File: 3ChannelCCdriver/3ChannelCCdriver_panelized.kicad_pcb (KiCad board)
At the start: 2 copper layers, 100.5 x 100.5 mm, 412 parts, among them J1 BB10-10S-02, J2 Screw_Terminal_01x02, J3 Screw_Terminal_01x02, J4 Screw_Terminal_01x02, J5 Screw_Terminal_01x02, U1 AL8860WT-7, U2 AL8860WT-7, U3 AL8860WT-7, U4 TPS54202DDC, U5 XL6019, U6 ESP-12F, U7 XC6210B332MR

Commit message: Added documentation
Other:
- board text added: "JLCJLCJLCJLC"

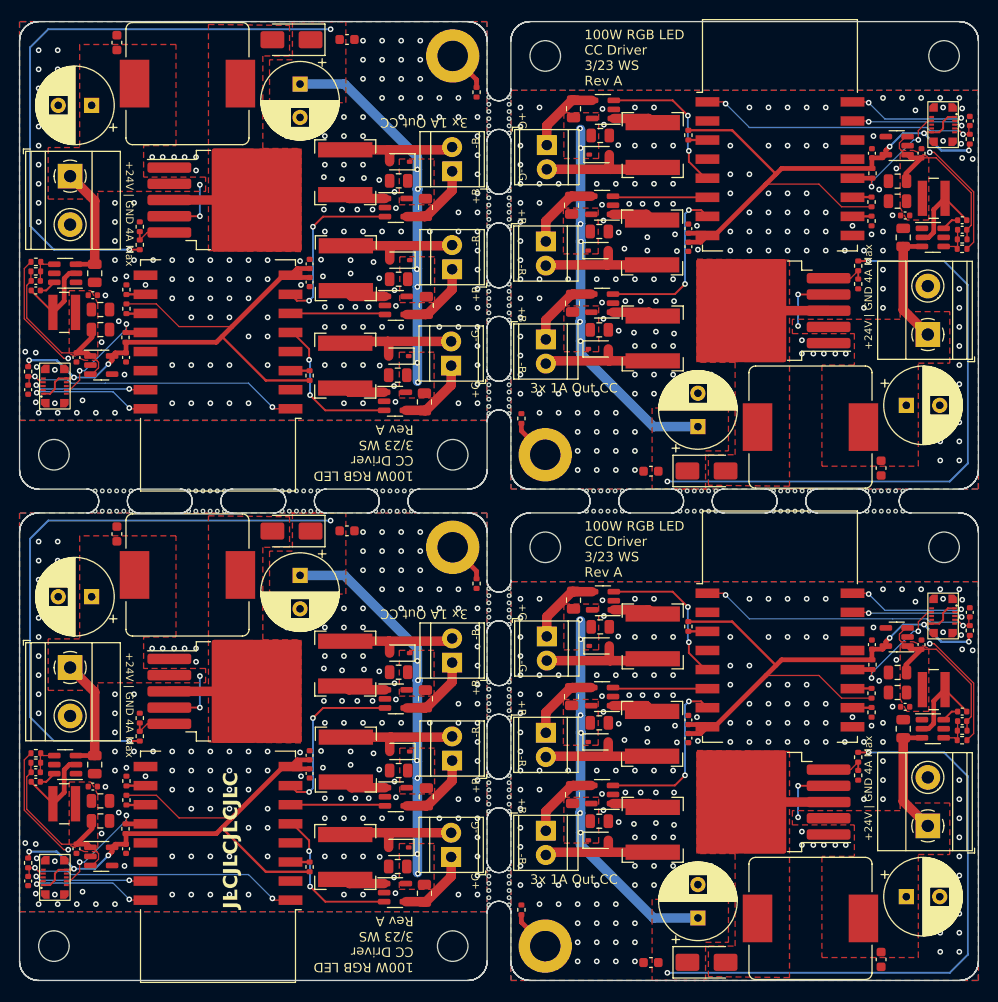
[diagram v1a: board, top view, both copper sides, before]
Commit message: changed panelization
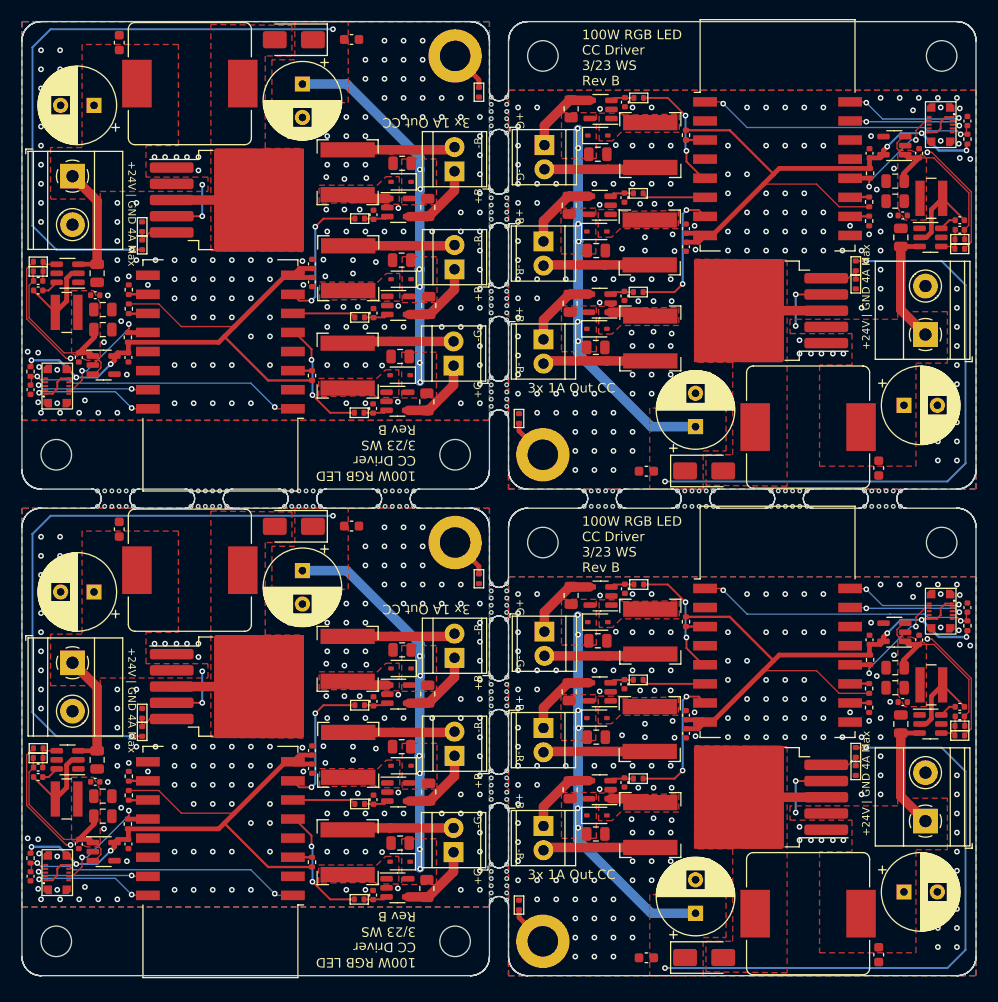
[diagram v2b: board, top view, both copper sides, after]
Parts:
- removed the C1 at (137.9, 57.1)
- removed the C1 at (159.1, 83.4)
- removed the C1 at (137.9, 108.6)
- removed the C1 at (159.1, 31.9)
- removed the C10 at (191.2, 60.2)
- removed the C10 at (105.8, 28.8)
- removed the C10 at (105.8, 80.3)
- removed the C10 at (191.2, 111.7)
- removed the C11 at (108.5, 73.7)
- removed the C11 at (108.5, 22.2)
- removed the C11 at (188.6, 118.3)
- removed the C11 at (188.6, 66.8)
- removed the C12 at (164.4, 118.6)
- removed the C12 at (132.6, 73.4)
- removed the C12 at (164.4, 67.1)
- removed the C12 at (132.6, 21.9)
- removed the C13 at (127.7, 26.5)
- removed the C13 at (127.7, 78.0)
- removed the C13 at (169.3, 114.0)
- removed the C13 at (169.3, 62.5)
- removed the C14 at (197.8, 30.4)
- removed the C14 at (197.8, 81.9)
- removed the C14 at (99.2, 58.6)
- removed the C14 at (99.2, 110.1)
- removed the C15 at (192.8, 85.3)
- removed the C15 at (104.2, 106.7)
- removed the C15 at (192.8, 33.8)
- removed the C15 at (104.2, 55.2)
- removed the C16 at (109.4, 55.2)
- removed the C16 at (187.6, 33.8)
- removed the C16 at (109.4, 106.7)
- removed the C16 at (187.6, 85.3)
- removed the C17 at (128.7, 45.4)
- removed the C17 at (128.7, 96.9)
- removed the C17 at (168.3, 43.6)
- removed the C17 at (168.3, 95.1)
- removed the C18 at (168.3, 93.2)
- removed the C18 at (168.3, 41.7)
- removed the C18 at (128.7, 98.8)
- removed the C18 at (128.7, 47.3)
- removed the C2 at (159.0, 93.5)
- removed the C2 at (138.0, 47.0)
- removed the C2 at (159.0, 42.0)
- removed the C2 at (138.0, 98.5)
- removed the C3 at (159.0, 52.3)
- removed the C3 at (159.0, 103.8)
- removed the C3 at (138.0, 88.2)
- removed the C3 at (138.0, 36.7)
- removed the C4 at (190.9, 94.1)
- removed the C4 at (190.9, 42.6)
- removed the C4 at (106.1, 46.4)
- removed the C4 at (106.1, 97.9)
- removed the C5 at (197.1, 92.3)
- removed the C5 at (100.0, 48.2)
- removed the C5 at (100.0, 99.7)
- removed the C5 at (197.1, 40.8)
- removed the C6 at (100.0, 98.7)
- removed the C6 at (197.1, 41.8)
- removed the C6 at (100.0, 47.2)
- removed the C6 at (197.1, 93.3)
- removed the C7 at (190.3, 88.2)
- removed the C7 at (106.7, 52.3)
- removed the C7 at (106.7, 103.8)
- removed the C7 at (190.3, 36.7)
- removed the C8 at (190.3, 90.3)
- removed the C8 at (106.7, 101.7)
- removed the C8 at (190.3, 38.8)
- removed the C8 at (106.7, 50.2)
- removed the C9 at (105.9, 100.2)
- removed the C9 at (191.1, 91.8)
- removed the C9 at (191.1, 40.3)
- removed the C9 at (105.9, 48.7)
- removed the D1 at (138.0, 106.6)
- removed the D1 at (159.0, 85.4)
- removed the D1 at (159.0, 33.9)
- removed the D1 at (138.0, 55.1)
- removed the D2 at (138.1, 96.5)
- removed the D2 at (138.1, 45.0)
- removed the D2 at (158.9, 44.0)
- removed the D2 at (158.9, 95.5)
- removed the D3 at (138.1, 34.7)
- removed the D3 at (158.9, 105.8)
- removed the D3 at (158.9, 54.3)
- removed the D3 at (138.1, 86.2)
- removed the D4 at (126.8, 73.4)
- removed the D4 at (170.2, 67.1)
- removed the D4 at (170.2, 118.6)
- removed the D4 at (126.8, 21.9)
- removed the H1 at (153.3, 116.9)
- removed the H1 at (153.3, 65.4)
- removed the H1 at (143.7, 23.6)
- removed the H1 at (143.7, 75.1)
- removed the H2 at (143.7, 116.9)
- removed the H2 at (153.3, 75.1)
- removed the H2 at (143.7, 65.4)
- removed the H2 at (153.3, 23.6)
- removed the H3 at (195.2, 75.1)
- removed the H3 at (195.2, 23.6)
- removed the H3 at (101.8, 116.9)
- removed the H3 at (101.8, 65.4)
- removed the J1 at (195.1, 30.8)
- removed the J1 at (195.1, 82.3)
- removed the J1 at (102.0, 58.2)
- removed the J1 at (102.0, 109.7)
- removed the J2 at (193.4, 52.8)
- removed the J2 at (103.5, 36.2)
- removed the J2 at (103.5, 87.7)
- removed the J2 at (193.4, 104.3)
- removed the J3 at (153.4, 94.5)
- removed the J3 at (153.4, 43.0)
- removed the J3 at (143.6, 97.5)
- removed the J3 at (143.6, 46.0)
- removed the J4 at (153.4, 104.8)
- removed the J4 at (143.6, 35.7)
- removed the J4 at (153.4, 53.3)
- removed the J4 at (143.6, 87.2)
- removed the J5 at (153.5, 32.9)
- removed the J5 at (143.5, 56.1)
- removed the J5 at (143.5, 107.6)
- removed the J5 at (153.5, 84.4)
- removed the L1 at (132.4, 56.1)
- removed the L1 at (164.6, 84.4)
- removed the L1 at (132.4, 107.6)
- removed the L1 at (164.6, 32.9)
- removed the L2 at (132.4, 45.9)
- removed the L2 at (132.4, 97.4)
- removed the L2 at (164.6, 43.1)
- removed the L2 at (164.6, 94.7)
- removed the L3 at (164.6, 53.2)
- removed the L3 at (164.6, 104.7)
- removed the L3 at (132.4, 87.3)
- removed the L3 at (132.4, 35.8)
- removed the L4 at (194.1, 38.5)
- removed the L4 at (102.9, 102.0)
- removed the L4 at (102.9, 50.5)
- removed the L4 at (194.1, 90.0)
- removed the L5 at (181.2, 114.0)
- removed the L5 at (115.8, 26.5)
- removed the L5 at (115.8, 78.0)
- removed the L5 at (181.2, 62.5)
- removed the R1 at (140.7, 111.4)
- removed the R1 at (156.3, 80.6)
- removed the R1 at (140.7, 59.9)
- removed the R1 at (156.3, 29.1)
- removed the R12 at (99.2, 56.7)
- removed the R12 at (197.8, 32.3)
- removed the R12 at (99.2, 108.2)
- removed the R12 at (197.8, 83.8)
- removed the R13 at (168.3, 83.4)
- removed the R13 at (168.3, 31.9)
- removed the R13 at (128.7, 108.6)
- removed the R13 at (128.7, 57.1)
- removed the R14 at (109.3, 53.1)
- removed the R14 at (187.7, 87.4)
- removed the R14 at (109.3, 104.6)
- removed the R14 at (187.7, 35.9)
- removed the R15 at (187.6, 38.9)
- removed the R15 at (187.6, 90.4)
- removed the R15 at (109.5, 50.1)
- removed the R15 at (109.5, 101.6)
- removed the R16 at (187.6, 40.9)
- removed the R16 at (187.6, 92.4)
- removed the R16 at (109.5, 99.6)
- removed the R16 at (109.5, 48.1)
- removed the R2 at (156.1, 39.2)
- removed the R2 at (140.9, 49.8)
- removed the R2 at (140.9, 101.3)
- removed the R2 at (156.1, 90.8)
- removed the R3 at (140.8, 91.0)
- removed the R3 at (156.2, 101.0)
- removed the R3 at (140.8, 39.5)
- removed the R3 at (156.2, 49.5)
- removed the R4 at (100.0, 97.7)
- removed the R4 at (100.0, 46.2)
- removed the R4 at (197.1, 42.8)
- removed the R4 at (197.1, 94.3)
- removed the R5 at (100.0, 96.7)
- removed the R5 at (100.0, 45.2)
- removed the R5 at (197.0, 95.3)
- removed the R5 at (197.0, 43.8)
- removed the R6 at (146.2, 78.9)
- removed the R6 at (146.2, 27.4)
- removed the R6 at (150.8, 61.6)
- removed the R6 at (150.8, 113.1)
- removed the R8 at (186.2, 45.6)
- removed the R8 at (110.8, 94.9)
- removed the R8 at (110.8, 43.4)
- removed the R8 at (186.2, 97.1)
- removed the R9 at (110.8, 93.0)
- removed the R9 at (186.2, 47.5)
- removed the R9 at (186.2, 99.0)
- removed the R9 at (110.8, 41.5)
- removed the REF** at (189.3, 69.2)
- removed the REF** at (167.5, 71.3)
- removed the REF** at (149.6, 111.1)
- removed the REF** at (149.6, 110.3)
- removed the REF** at (149.6, 100.5)
- removed the REF** at (147.4, 99.0)
- removed the REF** at (107.7, 69.2)
- removed the REF** at (179.5, 69.2)
- removed the REF** at (125.8, 71.3)
- removed the REF** at (178.0, 69.2)
- removed the REF** at (147.4, 29.4)
- removed the REF** at (157.7, 71.3)
- removed the REF** at (190.1, 71.3)
- removed the REF** at (149.6, 109.6)
- removed the REF** at (149.6, 80.9)
- removed the REF** at (160.7, 69.2)
- removed the REF** at (116.7, 71.3)
- removed the REF** at (147.4, 99.8)
- removed the REF** at (138.6, 69.2)
- removed the REF** at (147.4, 49.0)
- removed the REF** at (135.6, 69.2)
- removed the REF** at (161.4, 71.3)
- removed the REF** at (149.6, 108.8)
- removed the REF** at (149.6, 28.7)
- removed the REF** at (126.5, 71.3)
- removed the REF** at (147.4, 61.1)
- removed the REF** at (147.4, 82.4)
- removed the REF** at (147.4, 31.7)
- removed the REF** at (106.2, 69.2)
- removed the REF** at (147.4, 60.3)
- removed the REF** at (187.1, 69.2)
- removed the REF** at (147.4, 102.8)
- removed the REF** at (108.4, 71.3)
- removed the REF** at (116.0, 69.2)
- removed the REF** at (128.8, 71.3)
- removed the REF** at (147.4, 110.3)
- removed the REF** at (147.4, 40.7)
- removed the REF** at (187.1, 71.3)
- removed the REF** at (147.4, 89.2)
- removed the REF** at (137.1, 69.2)
- removed the REF** at (147.4, 59.6)
- removed the REF** at (147.4, 30.9)
- removed the REF** at (138.6, 71.3)
- removed the REF** at (119.7, 71.3)
- removed the REF** at (149.6, 47.5)
- removed the REF** at (128.0, 71.3)
- removed the REF** at (147.4, 37.7)
- removed the REF** at (109.2, 69.2)
- removed the REF** at (190.1, 69.2)
- removed the REF** at (106.2, 71.3)
- removed the REF** at (149.6, 39.2)
- removed the REF** at (128.0, 69.2)
- removed the REF** at (149.6, 30.2)
- removed the REF** at (147.4, 47.5)
- removed the REF** at (137.8, 71.3)
- removed the REF** at (149.6, 102.8)
- removed the REF** at (190.8, 69.2)
- removed the REF** at (167.5, 69.2)
- removed the REF** at (149.6, 102.0)
- removed the REF** at (168.2, 69.2)
- removed the REF** at (168.2, 71.3)
- removed the REF** at (171.2, 71.3)
- removed the REF** at (149.6, 80.2)
- removed the REF** at (149.6, 57.3)
- removed the REF** at (126.5, 69.2)
- removed the REF** at (147.4, 83.2)
- removed the REF** at (149.6, 81.7)
- removed the REF** at (147.4, 93.0)
- removed the REF** at (180.3, 69.2)
- removed the REF** at (149.6, 82.4)
- removed the REF** at (149.6, 31.7)
- removed the REF** at (147.4, 40.0)
- removed the REF** at (129.5, 69.2)
- removed the REF** at (147.4, 28.7)
- removed the REF** at (177.3, 71.3)
- removed the REF** at (149.6, 59.6)
- removed the REF** at (179.5, 71.3)
- removed the REF** at (149.6, 48.3)
- removed the REF** at (147.4, 79.4)
- removed the REF** at (147.4, 90.0)
- removed the REF** at (160.7, 71.3)
- removed the REF** at (169.7, 69.2)
- removed the REF** at (149.6, 61.1)
- removed the REF** at (149.6, 99.0)
- removed the REF** at (149.6, 93.0)
- removed the REF** at (159.9, 69.2)
- removed the REF** at (147.4, 102.0)
- removed the REF** at (181.0, 69.2)
- removed the REF** at (149.6, 49.8)
- removed the REF** at (149.6, 37.7)
- removed the REF** at (147.4, 50.5)
- removed the REF** at (117.5, 71.3)
- removed the REF** at (149.6, 51.3)
- removed the REF** at (188.6, 69.2)
- removed the REF** at (149.6, 99.8)
- removed the REF** at (136.3, 71.3)
- removed the REF** at (159.2, 71.3)
- removed the REF** at (147.4, 39.2)
- removed the REF** at (158.4, 69.2)
- removed the REF** at (181.0, 71.3)
- removed the REF** at (147.4, 100.5)
- removed the REF** at (149.6, 79.4)
- removed the REF** at (106.9, 69.2)
- removed the REF** at (137.1, 71.3)
- removed the REF** at (147.4, 109.6)
- removed the REF** at (147.4, 27.9)
- removed the REF** at (149.6, 27.9)
- removed the REF** at (147.4, 101.3)
- removed the REF** at (147.4, 58.8)
- removed the REF** at (119.0, 69.2)
- removed the REF** at (170.5, 69.2)
- removed the REF** at (149.6, 40.7)
- removed the REF** at (149.6, 91.5)
- removed the REF** at (169.0, 69.2)
- removed the REF** at (128.8, 69.2)
- removed the REF** at (116.7, 69.2)
- removed the REF** at (149.6, 38.5)
- removed the REF** at (147.4, 111.8)
- removed the REF** at (119.0, 71.3)
- removed the REF** at (149.6, 83.2)
- removed the REF** at (169.7, 71.3)
- removed the REF** at (147.4, 111.1)
- removed the REF** at (147.4, 49.8)
- removed the REF** at (107.7, 71.3)
- removed the REF** at (118.2, 69.2)
- removed the REF** at (147.4, 80.2)
- removed the REF** at (147.4, 38.5)
- removed the REF** at (149.6, 29.4)
- removed the REF** at (147.4, 92.2)
- removed the REF** at (147.4, 112.6)
- removed the REF** at (159.9, 71.3)
- removed the REF** at (178.8, 71.3)
- removed the REF** at (116.0, 71.3)
- removed the REF** at (147.4, 81.7)
- removed the REF** at (149.6, 58.8)
- removed the REF** at (177.3, 69.2)
- removed the REF** at (149.6, 41.5)
- removed the REF** at (137.8, 69.2)
- removed the REF** at (188.6, 71.3)
- removed the REF** at (169.0, 71.3)
- removed the REF** at (109.9, 69.2)
- removed the REF** at (149.6, 30.9)
- removed the REF** at (171.2, 69.2)
- removed the REF** at (178.8, 69.2)
- removed the REF** at (147.4, 57.3)
- removed the REF** at (106.9, 71.3)
- removed the REF** at (149.6, 89.2)
- removed the REF** at (149.6, 92.2)
- removed the REF** at (108.4, 69.2)
- removed the REF** at (136.3, 69.2)
- removed the REF** at (149.6, 90.7)
- removed the REF** at (117.5, 69.2)
- removed the REF** at (158.4, 71.3)
- removed the REF** at (127.3, 69.2)
- removed the REF** at (149.6, 58.1)
- removed the REF** at (127.3, 71.3)
- removed the REF** at (109.2, 71.3)
- removed the REF** at (170.5, 71.3)
- removed the REF** at (149.6, 112.6)
- removed the REF** at (147.4, 51.3)
- removed the REF** at (149.6, 101.3)
- removed the REF** at (149.6, 40.0)
- removed the REF** at (149.6, 90.0)
- removed the REF** at (147.4, 108.8)
- removed the REF** at (190.8, 71.3)
- removed the REF** at (187.8, 71.3)
- removed the REF** at (149.6, 60.3)
- removed the REF** at (139.3, 71.3)
- removed the REF** at (147.4, 41.5)
- removed the REF** at (118.2, 71.3)
- removed the REF** at (157.7, 69.2)
- removed the REF** at (149.6, 111.8)
- removed the REF** at (159.2, 69.2)
- removed the REF** at (147.4, 80.9)
- removed the REF** at (147.4, 58.1)
- removed the REF** at (149.6, 50.5)
- removed the REF** at (180.3, 71.3)
- removed the REF** at (147.4, 30.2)
- removed the REF** at (178.0, 71.3)
- removed the REF** at (161.4, 69.2)
- removed the REF** at (139.3, 69.2)
- removed the REF** at (149.6, 49.0)
- removed the REF** at (109.9, 71.3)
- removed the REF** at (147.4, 91.5)
- removed the REF** at (187.8, 69.2)
- removed the REF** at (189.3, 71.3)
- removed the REF** at (129.5, 71.3)
- removed the REF** at (147.4, 90.7)
- removed the REF** at (125.8, 69.2)
- removed the REF** at (147.4, 48.3)
- removed the REF** at (135.6, 71.3)
- removed the REF** at (119.7, 69.2)
- removed the U1 at (137.6, 111.3)
- removed the U1 at (137.6, 59.8)
- removed the U1 at (159.4, 29.2)
- removed the U1 at (159.4, 80.7)
- removed the U2 at (159.3, 90.8)
- removed the U2 at (159.3, 39.2)
- removed the U2 at (137.7, 49.8)
- removed the U2 at (137.7, 101.3)
- removed the U3 at (159.3, 101.0)
- removed the U3 at (137.7, 91.0)
- removed the U3 at (159.3, 49.5)
- removed the U3 at (137.7, 39.5)
- removed the U4 at (103.0, 46.4)
- removed the U4 at (194.0, 42.6)
- removed the U4 at (194.0, 94.1)
- removed the U4 at (103.0, 97.9)
- removed the U5 at (121.6, 38.7)
- removed the U5 at (121.6, 90.2)
- removed the U5 at (175.4, 50.3)
- removed the U5 at (175.4, 101.8)
- removed the U6 at (119.0, 57.1)
- removed the U6 at (177.9, 83.4)
- removed the U6 at (119.0, 108.6)
- removed the U6 at (177.9, 31.9)
- removed the U7 at (190.2, 33.0)
- removed the U7 at (106.8, 107.5)
- removed the U7 at (106.8, 56.0)
- removed the U7 at (190.2, 84.5)
- added C1: 0805,10uF,50V,X5R, Capacitor_SMD:C_0805_2012Metric, F.Cu at (158.9, 33.9)
- added C1: 0805,10uF,50V,X5R, Capacitor_SMD:C_0805_2012Metric, F.Cu at (138.1, 55.1)
- added C1: 0805,10uF,50V,X5R, Capacitor_SMD:C_0805_2012Metric, F.Cu at (158.9, 84.9)
- added C1: 0805,10uF,50V,X5R, Capacitor_SMD:C_0805_2012Metric, F.Cu at (138.1, 106.1)
- added C10: 220uF/50V, Capacitor_THT:CP_Radial_D8.0mm_P3.50mm, F.Cu at (106.1, 28.8)
- added C10: 220uF/50V, Capacitor_THT:CP_Radial_D8.0mm_P3.50mm, F.Cu at (190.9, 111.2)
- added C10: 220uF/50V, Capacitor_THT:CP_Radial_D8.0mm_P3.50mm, F.Cu at (190.9, 60.2)
- added C10: 220uF/50V, Capacitor_THT:CP_Radial_D8.0mm_P3.50mm, F.Cu at (106.1, 79.8)
- added C11: 0603,100nF,50V,X7R, Capacitor_SMD:C_0603_1608Metric, F.Cu at (188.3, 117.8)
- added C11: 0603,100nF,50V,X7R, Capacitor_SMD:C_0603_1608Metric, F.Cu at (108.7, 73.2)
- added C11: 0603,100nF,50V,X7R, Capacitor_SMD:C_0603_1608Metric, F.Cu at (108.7, 22.2)
- added C11: 0603,100nF,50V,X7R, Capacitor_SMD:C_0603_1608Metric, F.Cu at (188.3, 66.8)
- added C12: 0603,100nF,50V,X7R, Capacitor_SMD:C_0603_1608Metric, F.Cu at (133.1, 72.9)
- added C12: 0603,100nF,50V,X7R, Capacitor_SMD:C_0603_1608Metric, F.Cu at (133.1, 21.9)
- added C12: 0603,100nF,50V,X7R, Capacitor_SMD:C_0603_1608Metric, F.Cu at (163.9, 118.1)
- added C12: 0603,100nF,50V,X7R, Capacitor_SMD:C_0603_1608Metric, F.Cu at (163.9, 67.1)
- added C13: 220uF/50V, Capacitor_THT:CP_Radial_D8.0mm_P3.50mm, F.Cu at (169.1, 113.5)
- added C13: 220uF/50V, Capacitor_THT:CP_Radial_D8.0mm_P3.50mm, F.Cu at (127.9, 77.5)
- added C13: 220uF/50V, Capacitor_THT:CP_Radial_D8.0mm_P3.50mm, F.Cu at (127.9, 26.5)
- added C13: 220uF/50V, Capacitor_THT:CP_Radial_D8.0mm_P3.50mm, F.Cu at (169.1, 62.5)
- added C14: 100nF, Capacitor_SMD:C_0402_1005Metric, F.Cu at (99.4, 109.6)
- added C14: 100nF, Capacitor_SMD:C_0402_1005Metric, F.Cu at (197.6, 81.4)
- added C14: 100nF, Capacitor_SMD:C_0402_1005Metric, F.Cu at (197.6, 30.4)
- added C14: 100nF, Capacitor_SMD:C_0402_1005Metric, F.Cu at (99.4, 58.6)
- added C15: 10uF, Capacitor_SMD:C_0402_1005Metric, F.Cu at (104.5, 106.2)
- added C15: 10uF, Capacitor_SMD:C_0402_1005Metric, F.Cu at (192.5, 33.8)
- added C15: 10uF, Capacitor_SMD:C_0402_1005Metric, F.Cu at (192.5, 84.8)
- added C15: 10uF, Capacitor_SMD:C_0402_1005Metric, F.Cu at (104.5, 55.2)
- added C16: 10uF, Capacitor_SMD:C_0402_1005Metric, F.Cu at (109.7, 55.2)
- added C16: 10uF, Capacitor_SMD:C_0402_1005Metric, F.Cu at (187.3, 33.8)
- added C16: 10uF, Capacitor_SMD:C_0402_1005Metric, F.Cu at (187.3, 84.8)
- added C16: 10uF, Capacitor_SMD:C_0402_1005Metric, F.Cu at (109.7, 106.2)
- added C17: 10nF, Capacitor_SMD:C_0402_1005Metric, F.Cu at (128.9, 96.4)
- added C17: 10nF, Capacitor_SMD:C_0402_1005Metric, F.Cu at (168.1, 43.6)
- added C17: 10nF, Capacitor_SMD:C_0402_1005Metric, F.Cu at (128.9, 45.4)
- added C17: 10nF, Capacitor_SMD:C_0402_1005Metric, F.Cu at (168.1, 94.6)
- added C18: 100nF, Capacitor_SMD:C_0402_1005Metric, F.Cu at (128.9, 98.3)
- added C18: 100nF, Capacitor_SMD:C_0402_1005Metric, F.Cu at (168.1, 41.7)
- added C18: 100nF, Capacitor_SMD:C_0402_1005Metric, F.Cu at (128.9, 47.3)
- added C18: 100nF, Capacitor_SMD:C_0402_1005Metric, F.Cu at (168.1, 92.7)
- added C19: 0402,1uF,25V,X5R, Capacitor_SMD:C_0402_1005Metric, F.Cu at (135.3, 60.5)
- added C19: 0402,1uF,25V,X5R, Capacitor_SMD:C_0402_1005Metric, F.Cu at (161.7, 79.5)
- added C19: 0402,1uF,25V,X5R, Capacitor_SMD:C_0402_1005Metric, F.Cu at (161.7, 28.4)
- added C19: 0402,1uF,25V,X5R, Capacitor_SMD:C_0402_1005Metric, F.Cu at (135.3, 111.6)
- added C2: 0805,10uF,50V,X5R, Capacitor_SMD:C_0805_2012Metric, F.Cu at (158.7, 44.0)
- added C2: 0805,10uF,50V,X5R, Capacitor_SMD:C_0805_2012Metric, F.Cu at (138.3, 96.0)
- added C2: 0805,10uF,50V,X5R, Capacitor_SMD:C_0805_2012Metric, F.Cu at (138.3, 45.0)
- added C2: 0805,10uF,50V,X5R, Capacitor_SMD:C_0805_2012Metric, F.Cu at (158.7, 95.0)
- added C20: 0402,1uF,25V,X5R, Capacitor_SMD:C_0402_1005Metric, F.Cu at (135.3, 50.5)
- added C20: 0402,1uF,25V,X5R, Capacitor_SMD:C_0402_1005Metric, F.Cu at (161.7, 38.5)
- added C20: 0402,1uF,25V,X5R, Capacitor_SMD:C_0402_1005Metric, F.Cu at (161.7, 89.5)
- added C20: 0402,1uF,25V,X5R, Capacitor_SMD:C_0402_1005Metric, F.Cu at (135.3, 101.6)
- added C21: 0402,1uF,25V,X5R, Capacitor_SMD:C_0402_1005Metric, F.Cu at (135.3, 40.2)
- added C21: 0402,1uF,25V,X5R, Capacitor_SMD:C_0402_1005Metric, F.Cu at (161.7, 48.8)
- added C21: 0402,1uF,25V,X5R, Capacitor_SMD:C_0402_1005Metric, F.Cu at (161.7, 99.8)
- added C21: 0402,1uF,25V,X5R, Capacitor_SMD:C_0402_1005Metric, F.Cu at (135.3, 91.3)
- added C3: 0805,10uF,50V,X5R, Capacitor_SMD:C_0805_2012Metric, F.Cu at (138.3, 34.9)
- added C3: 0805,10uF,50V,X5R, Capacitor_SMD:C_0805_2012Metric, F.Cu at (158.7, 105.2)
- added C3: 0805,10uF,50V,X5R, Capacitor_SMD:C_0805_2012Metric, F.Cu at (158.7, 54.1)
- added C3: 0805,10uF,50V,X5R, Capacitor_SMD:C_0805_2012Metric, F.Cu at (138.3, 85.9)
- added C4: 0805,10uF,50V,X5R, Capacitor_SMD:C_0805_2012Metric, F.Cu at (106.4, 97.4)
- added C4: 0805,10uF,50V,X5R, Capacitor_SMD:C_0805_2012Metric, F.Cu at (190.6, 42.6)
- added C4: 0805,10uF,50V,X5R, Capacitor_SMD:C_0805_2012Metric, F.Cu at (190.6, 93.6)
- added C4: 0805,10uF,50V,X5R, Capacitor_SMD:C_0805_2012Metric, F.Cu at (106.4, 46.4)
- added C5: 0402,100nF,16V,X7R, Capacitor_SMD:C_0402_1005Metric, F.Cu at (100.2, 48.2)
- added C5: 0402,100nF,16V,X7R, Capacitor_SMD:C_0402_1005Metric, F.Cu at (196.8, 40.8)
- added C5: 0402,100nF,16V,X7R, Capacitor_SMD:C_0402_1005Metric, F.Cu at (196.8, 91.8)
- added C5: 0402,100nF,16V,X7R, Capacitor_SMD:C_0402_1005Metric, F.Cu at (100.2, 99.2)
- added C6: 0402,100pF,50V,C0G, Capacitor_SMD:C_0402_1005Metric, F.Cu at (196.8, 92.8)
- added C6: 0402,100pF,50V,C0G, Capacitor_SMD:C_0402_1005Metric, F.Cu at (100.2, 47.2)
- added C6: 0402,100pF,50V,C0G, Capacitor_SMD:C_0402_1005Metric, F.Cu at (100.2, 98.2)
- added C6: 0402,100pF,50V,C0G, Capacitor_SMD:C_0402_1005Metric, F.Cu at (196.8, 41.8)
- added C7: 0805,47uF,6.3V,X5R, Capacitor_SMD:C_0805_2012Metric, F.Cu at (190.0, 36.7)
- added C7: 0805,47uF,6.3V,X5R, Capacitor_SMD:C_0805_2012Metric, F.Cu at (190.0, 87.7)
- added C7: 0805,47uF,6.3V,X5R, Capacitor_SMD:C_0805_2012Metric, F.Cu at (107.0, 103.3)
- added C7: 0805,47uF,6.3V,X5R, Capacitor_SMD:C_0805_2012Metric, F.Cu at (107.0, 52.3)
- added C8: 0805,47uF,6.3V,X5R, Capacitor_SMD:C_0805_2012Metric, F.Cu at (190.0, 38.8)
- added C8: 0805,47uF,6.3V,X5R, Capacitor_SMD:C_0805_2012Metric, F.Cu at (107.0, 101.2)
- added C8: 0805,47uF,6.3V,X5R, Capacitor_SMD:C_0805_2012Metric, F.Cu at (190.0, 89.8)
- added C8: 0805,47uF,6.3V,X5R, Capacitor_SMD:C_0805_2012Metric, F.Cu at (107.0, 50.2)
- added C9: 0402,330pF,50V,C0G, Capacitor_SMD:C_0402_1005Metric, F.Cu at (106.2, 99.7)
- added C9: 0402,330pF,50V,C0G, Capacitor_SMD:C_0402_1005Metric, F.Cu at (106.2, 48.7)
- added C9: 0402,330pF,50V,C0G, Capacitor_SMD:C_0402_1005Metric, F.Cu at (190.8, 40.3)
- added C9: 0402,330pF,50V,C0G, Capacitor_SMD:C_0402_1005Metric, F.Cu at (190.8, 91.3)
- added D1: 1N5819WS, Diode_SMD:D_SOD-323, F.Cu at (158.9, 31.9)
- added D1: 1N5819WS, Diode_SMD:D_SOD-323, F.Cu at (158.9, 82.9)
- added D1: 1N5819WS, Diode_SMD:D_SOD-323, F.Cu at (138.1, 57.1)
- added D1: 1N5819WS, Diode_SMD:D_SOD-323, F.Cu at (138.1, 108.1)
- added D2: 1N5819WS, Diode_SMD:D_SOD-323, F.Cu at (158.8, 42.0)
- added D2: 1N5819WS, Diode_SMD:D_SOD-323, F.Cu at (138.2, 98.0)
- added D2: 1N5819WS, Diode_SMD:D_SOD-323, F.Cu at (138.2, 47.0)
- added D2: 1N5819WS, Diode_SMD:D_SOD-323, F.Cu at (158.8, 93.0)
- added D3: 1N5819WS, Diode_SMD:D_SOD-323, F.Cu at (138.2, 36.8)
- added D3: 1N5819WS, Diode_SMD:D_SOD-323, F.Cu at (138.2, 87.8)
- added D3: 1N5819WS, Diode_SMD:D_SOD-323, F.Cu at (158.8, 103.2)
- added D3: 1N5819WS, Diode_SMD:D_SOD-323, F.Cu at (158.8, 52.2)
- added D4: SS54, Diode_SMD:D_SMA, F.Cu at (127.0, 72.9)
- added D4: SS54, Diode_SMD:D_SMA, F.Cu at (170.0, 118.1)
- added D4: SS54, Diode_SMD:D_SMA, F.Cu at (170.0, 67.1)
- added D4: SS54, Diode_SMD:D_SMA, F.Cu at (127.0, 21.9)
- added H1: MountingHole_Pad, MountingHole:MountingHole_3.2mm_M3_DIN965_Pad, F.Cu at (143.9, 23.6)
- added H1: MountingHole_Pad, MountingHole:MountingHole_3.2mm_M3_DIN965_Pad, F.Cu at (143.9, 74.6)
- added H1: MountingHole_Pad, MountingHole:MountingHole_3.2mm_M3_DIN965_Pad, F.Cu at (153.1, 65.4)
- added H1: MountingHole_Pad, MountingHole:MountingHole_3.2mm_M3_DIN965_Pad, F.Cu at (153.1, 116.4)
- added H2: MountingHole, MountingHole:MountingHole_3.2mm_M3, F.Cu at (143.9, 65.4)
- added H2: MountingHole, MountingHole:MountingHole_3.2mm_M3, F.Cu at (143.9, 116.4)
- added H2: MountingHole, MountingHole:MountingHole_3.2mm_M3, F.Cu at (153.1, 23.6)
- added H2: MountingHole, MountingHole:MountingHole_3.2mm_M3, F.Cu at (153.1, 74.6)
- added H3: MountingHole, MountingHole:MountingHole_3.2mm_M3, F.Cu at (102.1, 116.4)
- added H3: MountingHole, MountingHole:MountingHole_3.2mm_M3, F.Cu at (194.9, 74.6)
- added H3: MountingHole, MountingHole:MountingHole_3.2mm_M3, F.Cu at (194.9, 23.6)
- added H3: MountingHole, MountingHole:MountingHole_3.2mm_M3, F.Cu at (102.1, 65.4)
- added J1: BB10-10S-02, WS_LCSC_Connectors:YXT-BB10-10S-02, F.Cu at (194.8, 81.8)
- added J1: BB10-10S-02, WS_LCSC_Connectors:YXT-BB10-10S-02, F.Cu at (194.8, 30.8)
- added J1: BB10-10S-02, WS_LCSC_Connectors:YXT-BB10-10S-02, F.Cu at (102.2, 58.2)
- added J1: BB10-10S-02, WS_LCSC_Connectors:YXT-BB10-10S-02, F.Cu at (102.2, 109.2)
- added J2: Screw_Terminal_01x02, TerminalBlock_Phoenix:TerminalBlock_Phoenix_MKDS-1,5-2-5.08_1x02_P5.08mm_Horizontal, F.Cu at (103.8, 36.2)
- added J2: Screw_Terminal_01x02, TerminalBlock_Phoenix:TerminalBlock_Phoenix_MKDS-1,5-2-5.08_1x02_P5.08mm_Horizontal, F.Cu at (103.8, 87.2)
- added J2: Screw_Terminal_01x02, TerminalBlock_Phoenix:TerminalBlock_Phoenix_MKDS-1,5-2-5.08_1x02_P5.08mm_Horizontal, F.Cu at (193.2, 52.8)
- added J2: Screw_Terminal_01x02, TerminalBlock_Phoenix:TerminalBlock_Phoenix_MKDS-1,5-2-5.08_1x02_P5.08mm_Horizontal, F.Cu at (193.2, 103.8)
- added J3: Screw_Terminal_01x02, TerminalBlock_TE-Connectivity:TerminalBlock_TE_282834-2_1x02_P2.54mm_Horizontal, F.Cu at (143.8, 97.0)
- added J3: Screw_Terminal_01x02, TerminalBlock_TE-Connectivity:TerminalBlock_TE_282834-2_1x02_P2.54mm_Horizontal, F.Cu at (153.2, 94.0)
- added J3: Screw_Terminal_01x02, TerminalBlock_TE-Connectivity:TerminalBlock_TE_282834-2_1x02_P2.54mm_Horizontal, F.Cu at (143.8, 46.0)
- added J3: Screw_Terminal_01x02, TerminalBlock_TE-Connectivity:TerminalBlock_TE_282834-2_1x02_P2.54mm_Horizontal, F.Cu at (153.2, 43.0)
- added J4: Screw_Terminal_01x02, TerminalBlock_TE-Connectivity:TerminalBlock_TE_282834-2_1x02_P2.54mm_Horizontal, F.Cu at (153.2, 104.3)
- added J4: Screw_Terminal_01x02, TerminalBlock_TE-Connectivity:TerminalBlock_TE_282834-2_1x02_P2.54mm_Horizontal, F.Cu at (143.8, 86.7)
- added J4: Screw_Terminal_01x02, TerminalBlock_TE-Connectivity:TerminalBlock_TE_282834-2_1x02_P2.54mm_Horizontal, F.Cu at (143.8, 35.7)
- added J4: Screw_Terminal_01x02, TerminalBlock_TE-Connectivity:TerminalBlock_TE_282834-2_1x02_P2.54mm_Horizontal, F.Cu at (153.2, 53.3)
- added J5: Screw_Terminal_01x02, TerminalBlock_TE-Connectivity:TerminalBlock_TE_282834-2_1x02_P2.54mm_Horizontal, F.Cu at (143.7, 107.1)
- added J5: Screw_Terminal_01x02, TerminalBlock_TE-Connectivity:TerminalBlock_TE_282834-2_1x02_P2.54mm_Horizontal, F.Cu at (143.7, 56.1)
- added J5: Screw_Terminal_01x02, TerminalBlock_TE-Connectivity:TerminalBlock_TE_282834-2_1x02_P2.54mm_Horizontal, F.Cu at (153.3, 32.9)
- added J5: Screw_Terminal_01x02, TerminalBlock_TE-Connectivity:TerminalBlock_TE_282834-2_1x02_P2.54mm_Horizontal, F.Cu at (153.3, 83.9)
- added L1: 33uH/1.45A, Inductor_SMD:L_Bourns-SRN6028, F.Cu at (164.4, 83.9)
- added L1: 33uH/1.45A, Inductor_SMD:L_Bourns-SRN6028, F.Cu at (132.6, 56.1)
- added L1: 33uH/1.45A, Inductor_SMD:L_Bourns-SRN6028, F.Cu at (164.4, 32.9)
- added L1: 33uH/1.45A, Inductor_SMD:L_Bourns-SRN6028, F.Cu at (132.6, 107.1)
- added L2: 33uH/1.45A, Inductor_SMD:L_Bourns-SRN6028, F.Cu at (132.7, 45.9)
- added L2: 33uH/1.45A, Inductor_SMD:L_Bourns-SRN6028, F.Cu at (164.3, 43.1)
- added L2: 33uH/1.45A, Inductor_SMD:L_Bourns-SRN6028, F.Cu at (132.7, 96.9)
- added L2: 33uH/1.45A, Inductor_SMD:L_Bourns-SRN6028, F.Cu at (164.3, 94.2)
- added L3: 33uH/1.45A, Inductor_SMD:L_Bourns-SRN6028, F.Cu at (132.6, 35.8)
- added L3: 33uH/1.45A, Inductor_SMD:L_Bourns-SRN6028, F.Cu at (164.4, 53.2)
- added L3: 33uH/1.45A, Inductor_SMD:L_Bourns-SRN6028, F.Cu at (164.4, 104.2)
- added L3: 33uH/1.45A, Inductor_SMD:L_Bourns-SRN6028, F.Cu at (132.6, 86.8)
- added L4: 4.7uH/2A, Inductor_SMD:L_Wuerth_MAPI-4030, F.Cu at (193.8, 89.5)
- added L4: 4.7uH/2A, Inductor_SMD:L_Wuerth_MAPI-4030, F.Cu at (103.2, 50.5)
- added L4: 4.7uH/2A, Inductor_SMD:L_Wuerth_MAPI-4030, F.Cu at (103.2, 101.5)
- added L4: 4.7uH/2A, Inductor_SMD:L_Wuerth_MAPI-4030, F.Cu at (193.8, 38.5)
- added L5: 47uH/5A, Inductor_SMD:L_Bourns_SRP1245A, F.Cu at (116.1, 77.5)
- added L5: 47uH/5A, Inductor_SMD:L_Bourns_SRP1245A, F.Cu at (116.1, 26.5)
- added L5: 47uH/5A, Inductor_SMD:L_Bourns_SRP1245A, F.Cu at (180.9, 113.5)
- added L5: 47uH/5A, Inductor_SMD:L_Bourns_SRP1245A, F.Cu at (180.9, 62.5)
- added R1: 0.1R/0.25W, Resistor_SMD:R_0805_2012Metric, F.Cu at (140.9, 110.9)
- added R1: 0.1R/0.25W, Resistor_SMD:R_0805_2012Metric, F.Cu at (156.1, 80.1)
- added R1: 0.1R/0.25W, Resistor_SMD:R_0805_2012Metric, F.Cu at (140.9, 59.9)
- added R1: 0.1R/0.25W, Resistor_SMD:R_0805_2012Metric, F.Cu at (156.1, 29.1)
- added R10: 0402,4.7k, PCM_Resistor_SMD_AKL:R_0402_1005Metric, F.Cu at (163.1, 89.0)
- added R10: 0402,4.7k, PCM_Resistor_SMD_AKL:R_0402_1005Metric, F.Cu at (163.1, 38.0)
- added R10: 0402,4.7k, PCM_Resistor_SMD_AKL:R_0402_1005Metric, F.Cu at (133.9, 51.0)
- added R10: 0402,4.7k, PCM_Resistor_SMD_AKL:R_0402_1005Metric, F.Cu at (133.9, 102.0)
- added R11: 0402,4.7k, PCM_Resistor_SMD_AKL:R_0402_1005Metric, F.Cu at (163.1, 48.4)
- added R11: 0402,4.7k, PCM_Resistor_SMD_AKL:R_0402_1005Metric, F.Cu at (163.1, 99.4)
- added R11: 0402,4.7k, PCM_Resistor_SMD_AKL:R_0402_1005Metric, F.Cu at (133.9, 40.6)
- added R11: 0402,4.7k, PCM_Resistor_SMD_AKL:R_0402_1005Metric, F.Cu at (133.9, 91.7)
- added R12: 10K, Resistor_SMD:R_0402_1005Metric, F.Cu at (197.6, 32.3)
- added R12: 10K, Resistor_SMD:R_0402_1005Metric, F.Cu at (99.4, 56.7)
- added R12: 10K, Resistor_SMD:R_0402_1005Metric, F.Cu at (99.4, 107.7)
- added R12: 10K, Resistor_SMD:R_0402_1005Metric, F.Cu at (197.6, 83.3)
- added R13: 10K, Resistor_SMD:R_0402_1005Metric, F.Cu at (128.9, 108.1)
- added R13: 10K, Resistor_SMD:R_0402_1005Metric, F.Cu at (168.1, 31.9)
- added R13: 10K, Resistor_SMD:R_0402_1005Metric, F.Cu at (168.1, 82.9)
- added R13: 10K, Resistor_SMD:R_0402_1005Metric, F.Cu at (128.9, 57.1)
- added R14: 10K, Resistor_SMD:R_0402_1005Metric, F.Cu at (187.4, 86.9)
- added R14: 10K, Resistor_SMD:R_0402_1005Metric, F.Cu at (109.6, 53.1)
- added R14: 10K, Resistor_SMD:R_0402_1005Metric, F.Cu at (109.6, 104.1)
- added R14: 10K, Resistor_SMD:R_0402_1005Metric, F.Cu at (187.4, 35.9)
- added R15: 10K, Resistor_SMD:R_0402_1005Metric, F.Cu at (187.3, 89.9)
- added R15: 10K, Resistor_SMD:R_0402_1005Metric, F.Cu at (109.7, 101.1)
- added R15: 10K, Resistor_SMD:R_0402_1005Metric, F.Cu at (109.7, 50.1)
- added R15: 10K, Resistor_SMD:R_0402_1005Metric, F.Cu at (187.3, 38.9)
- added R16: 10K, Resistor_SMD:R_0402_1005Metric, F.Cu at (109.7, 48.1)
- added R16: 10K, Resistor_SMD:R_0402_1005Metric, F.Cu at (187.3, 40.9)
- added R16: 10K, Resistor_SMD:R_0402_1005Metric, F.Cu at (187.3, 91.9)
- added R16: 10K, Resistor_SMD:R_0402_1005Metric, F.Cu at (109.7, 99.1)
- added R2: 0.1R/0.25W, Resistor_SMD:R_0805_2012Metric, F.Cu at (141.1, 49.8)
- added R2: 0.1R/0.25W, Resistor_SMD:R_0805_2012Metric, F.Cu at (155.9, 39.2)
- added R2: 0.1R/0.25W, Resistor_SMD:R_0805_2012Metric, F.Cu at (155.9, 90.3)
- added R2: 0.1R/0.25W, Resistor_SMD:R_0805_2012Metric, F.Cu at (141.1, 100.8)
- added R3: 0.1R/0.25W, Resistor_SMD:R_0805_2012Metric, F.Cu at (141.0, 39.5)
- added R3: 0.1R/0.25W, Resistor_SMD:R_0805_2012Metric, F.Cu at (141.0, 90.5)
- added R3: 0.1R/0.25W, Resistor_SMD:R_0805_2012Metric, F.Cu at (156.0, 49.5)
- added R3: 0.1R/0.25W, Resistor_SMD:R_0805_2012Metric, F.Cu at (156.0, 100.5)
- added R4: 0402,100k, PCM_Resistor_SMD_AKL:R_0402_1005Metric, F.Cu at (100.2, 97.2)
- added R4: 0402,100k, PCM_Resistor_SMD_AKL:R_0402_1005Metric, F.Cu at (100.2, 46.2)
- added R4: 0402,100k, PCM_Resistor_SMD_AKL:R_0402_1005Metric, F.Cu at (196.8, 42.8)
- added R4: 0402,100k, PCM_Resistor_SMD_AKL:R_0402_1005Metric, F.Cu at (196.8, 93.8)
- added R5: 0402,15k, PCM_Resistor_SMD_AKL:R_0402_1005Metric, F.Cu at (100.2, 45.2)
- added R5: 0402,15k, PCM_Resistor_SMD_AKL:R_0402_1005Metric, F.Cu at (100.2, 96.2)
- added R5: 0402,15k, PCM_Resistor_SMD_AKL:R_0402_1005Metric, F.Cu at (196.8, 43.8)
- added R5: 0402,15k, PCM_Resistor_SMD_AKL:R_0402_1005Metric, F.Cu at (196.8, 94.8)
- added R6: 0402,0, PCM_Resistor_SMD_AKL:R_0402_1005Metric, F.Cu at (150.6, 61.6)
- added R6: 0402,0, PCM_Resistor_SMD_AKL:R_0402_1005Metric, F.Cu at (150.6, 112.6)
- added R6: 0402,0, PCM_Resistor_SMD_AKL:R_0402_1005Metric, F.Cu at (146.4, 78.4)
- added R6: 0402,0, PCM_Resistor_SMD_AKL:R_0402_1005Metric, F.Cu at (146.4, 27.4)
- added R7: 0402,4.7k, PCM_Resistor_SMD_AKL:R_0402_1005Metric, F.Cu at (133.8, 61.0)
- added R7: 0402,4.7k, PCM_Resistor_SMD_AKL:R_0402_1005Metric, F.Cu at (163.2, 28.0)
- added R7: 0402,4.7k, PCM_Resistor_SMD_AKL:R_0402_1005Metric, F.Cu at (133.8, 112.0)
- added R7: 0402,4.7k, PCM_Resistor_SMD_AKL:R_0402_1005Metric, F.Cu at (163.2, 79.0)
- added R8: 0402,56k, PCM_Resistor_SMD_AKL:R_0402_1005Metric, F.Cu at (185.9, 45.6)
- added R8: 0402,56k, PCM_Resistor_SMD_AKL:R_0402_1005Metric, F.Cu at (111.1, 43.4)
- added R8: 0402,56k, PCM_Resistor_SMD_AKL:R_0402_1005Metric, F.Cu at (111.1, 94.4)
- added R8: 0402,56k, PCM_Resistor_SMD_AKL:R_0402_1005Metric, F.Cu at (185.9, 96.6)
- added R9: 0402,2k, PCM_Resistor_SMD_AKL:R_0402_1005Metric, F.Cu at (111.1, 41.5)
- added R9: 0402,2k, PCM_Resistor_SMD_AKL:R_0402_1005Metric, F.Cu at (185.9, 47.5)
- added R9: 0402,2k, PCM_Resistor_SMD_AKL:R_0402_1005Metric, F.Cu at (111.1, 92.5)
- added R9: 0402,2k, PCM_Resistor_SMD_AKL:R_0402_1005Metric, F.Cu at (185.9, 98.5)
- added REF**: NPTH, NPTH, F.Cu at (117.7, 70.8)
- added REF**: NPTH, NPTH, F.Cu at (147.7, 91.7)
- added REF**: NPTH, NPTH, F.Cu at (177.0, 69.2)
- added REF**: NPTH, NPTH, F.Cu at (147.7, 101.5)
- added REF**: NPTH, NPTH, F.Cu at (139.6, 69.2)
- added REF**: NPTH, NPTH, F.Cu at (149.3, 81.9)
- added REF**: NPTH, NPTH, F.Cu at (147.7, 99.3)
- added REF**: NPTH, NPTH, F.Cu at (189.1, 70.8)
- added REF**: NPTH, NPTH, F.Cu at (149.3, 98.5)
- added REF**: NPTH, NPTH, F.Cu at (190.6, 70.8)
- added REF**: NPTH, NPTH, F.Cu at (149.3, 110.6)
- added REF**: NPTH, NPTH, F.Cu at (180.8, 69.2)
- added REF**: NPTH, NPTH, F.Cu at (117.0, 70.8)
- added REF**: NPTH, NPTH, F.Cu at (187.6, 69.2)
- added REF**: NPTH, NPTH, F.Cu at (129.0, 70.8)
- added REF**: NPTH, NPTH, F.Cu at (180.0, 69.2)
- added REF**: NPTH, NPTH, F.Cu at (147.7, 28.7)
- added REF**: NPTH, NPTH, F.Cu at (147.7, 38.5)
- added REF**: NPTH, NPTH, F.Cu at (137.3, 70.8)
- added REF**: NPTH, NPTH, F.Cu at (149.3, 80.4)
- added REF**: NPTH, NPTH, F.Cu at (147.7, 27.9)
- added REF**: NPTH, NPTH, F.Cu at (126.8, 70.8)
- added REF**: NPTH, NPTH, F.Cu at (158.2, 70.8)
- added REF**: NPTH, NPTH, F.Cu at (138.1, 69.2)
- added REF**: NPTH, NPTH, F.Cu at (119.2, 70.8)
- added REF**: NPTH, NPTH, F.Cu at (135.8, 70.8)
- added REF**: NPTH, NPTH, F.Cu at (167.2, 70.8)
- added REF**: NPTH, NPTH, F.Cu at (118.5, 69.2)
- added REF**: NPTH, NPTH, F.Cu at (177.8, 70.8)
- added REF**: NPTH, NPTH, F.Cu at (147.7, 37.7)
- added REF**: NPTH, NPTH, F.Cu at (147.7, 92.5)
- added REF**: NPTH, NPTH, F.Cu at (149.3, 47.5)
- added REF**: NPTH, NPTH, F.Cu at (149.3, 58.1)
- added REF**: NPTH, NPTH, F.Cu at (147.7, 51.3)
- added REF**: NPTH, NPTH, F.Cu at (178.5, 70.8)
- added REF**: NPTH, NPTH, F.Cu at (107.9, 69.2)
- added REF**: NPTH, NPTH, F.Cu at (110.2, 69.2)
- added REF**: NPTH, NPTH, F.Cu at (169.5, 70.8)
- added REF**: NPTH, NPTH, F.Cu at (128.3, 70.8)
- added REF**: NPTH, NPTH, F.Cu at (147.7, 100.8)
- added REF**: NPTH, NPTH, F.Cu at (147.7, 40.0)
- added REF**: NPTH, NPTH, F.Cu at (157.4, 69.2)
- added REF**: NPTH, NPTH, F.Cu at (189.8, 69.2)
- added REF**: NPTH, NPTH, F.Cu at (108.7, 70.8)
- added REF**: NPTH, NPTH, F.Cu at (168.7, 70.8)
- added REF**: NPTH, NPTH, F.Cu at (147.7, 112.1)
- added REF**: NPTH, NPTH, F.Cu at (159.7, 70.8)
- added REF**: NPTH, NPTH, F.Cu at (149.3, 78.9)
- added REF**: NPTH, NPTH, F.Cu at (188.3, 70.8)
- added REF**: NPTH, NPTH, F.Cu at (147.7, 91.0)
- added REF**: NPTH, NPTH, F.Cu at (149.3, 49.0)
- added REF**: NPTH, NPTH, F.Cu at (147.7, 58.8)
- added REF**: NPTH, NPTH, F.Cu at (117.7, 69.2)
- added REF**: NPTH, NPTH, F.Cu at (189.8, 70.8)
- added REF**: NPTH, NPTH, F.Cu at (126.0, 70.8)
- added REF**: NPTH, NPTH, F.Cu at (149.3, 40.7)
- added REF**: NPTH, NPTH, F.Cu at (147.7, 61.1)
- added REF**: NPTH, NPTH, F.Cu at (149.3, 91.7)
- added REF**: NPTH, NPTH, F.Cu at (126.0, 69.2)
- added REF**: NPTH, NPTH, F.Cu at (116.2, 70.8)
- added REF**: NPTH, NPTH, F.Cu at (171.0, 69.2)
- added REF**: NPTH, NPTH, F.Cu at (178.5, 69.2)
- added REF**: NPTH, NPTH, F.Cu at (149.3, 108.3)
- added REF**: NPTH, NPTH, F.Cu at (189.1, 69.2)
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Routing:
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- added copper zone on F.Cu, net Board_0-/CCDriver_1Ch1/SW
- added copper zone on F.Cu, net Board_0-/CCDriver_1Ch2/SW
- added copper zone on F.Cu, net Board_0-/CCDriver_1Ch3/SW
- added copper zone on F.Cu, net Board_1-/CCDriver_1Ch1/SW
- added copper zone on F.Cu, net Board_1-/CCDriver_1Ch2/SW
- added copper zone on F.Cu, net Board_1-/CCDriver_1Ch3/SW
- added copper zone on F.Cu, net Board_2-/CCDriver_1Ch1/SW
- added copper zone on F.Cu, net Board_2-/CCDriver_1Ch2/SW
- added copper zone on F.Cu, net Board_2-/CCDriver_1Ch3/SW
- added copper zone on F.Cu, net Board_3-/CCDriver_1Ch1/SW
- added copper zone on F.Cu, net Board_3-/CCDriver_1Ch2/SW
- added copper zone on F.Cu, net Board_3-/CCDriver_1Ch3/SW
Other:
- board size 100.5 x 100.5 mm -> 100 x 100 mm
- board text added: "100W RGB LED CC Driver 3/23 WS Rev B"
- board text removed: "100W RGB LED CC Driver 3/23 WS Rev A"
- board text removed: "JLCJLCJLCJLC"
